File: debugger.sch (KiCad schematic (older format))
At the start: 12 parts, among them J2 USB_B_Micro, J5 Conn_ARM_JTAG_SWD_10, J6 Conn_ARM_JTAG_SWD_10, U7 STM32F042F6Px

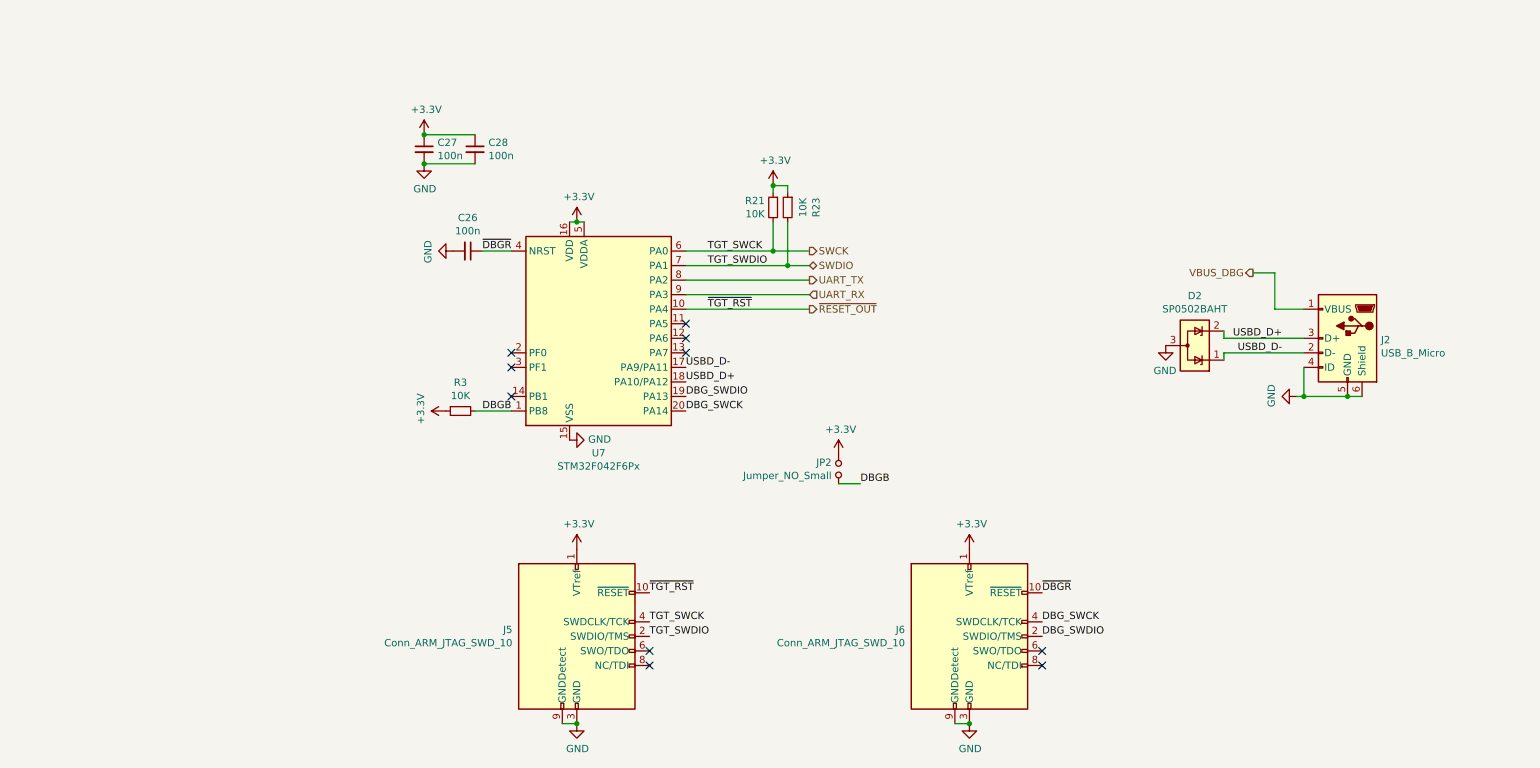
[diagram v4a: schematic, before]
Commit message: Replace STM32F042 in TSSOP by STM32F04[28] in QFN28
Others changes:

 - Export gerbers to current status
 - Update schematic export in svg and pdf
 - Update README image
 - Rename `USB OTG` sheet to `USB_OTG`

Signed-off-by: Martin Ribelotta <martinribelotta@gmail.com>
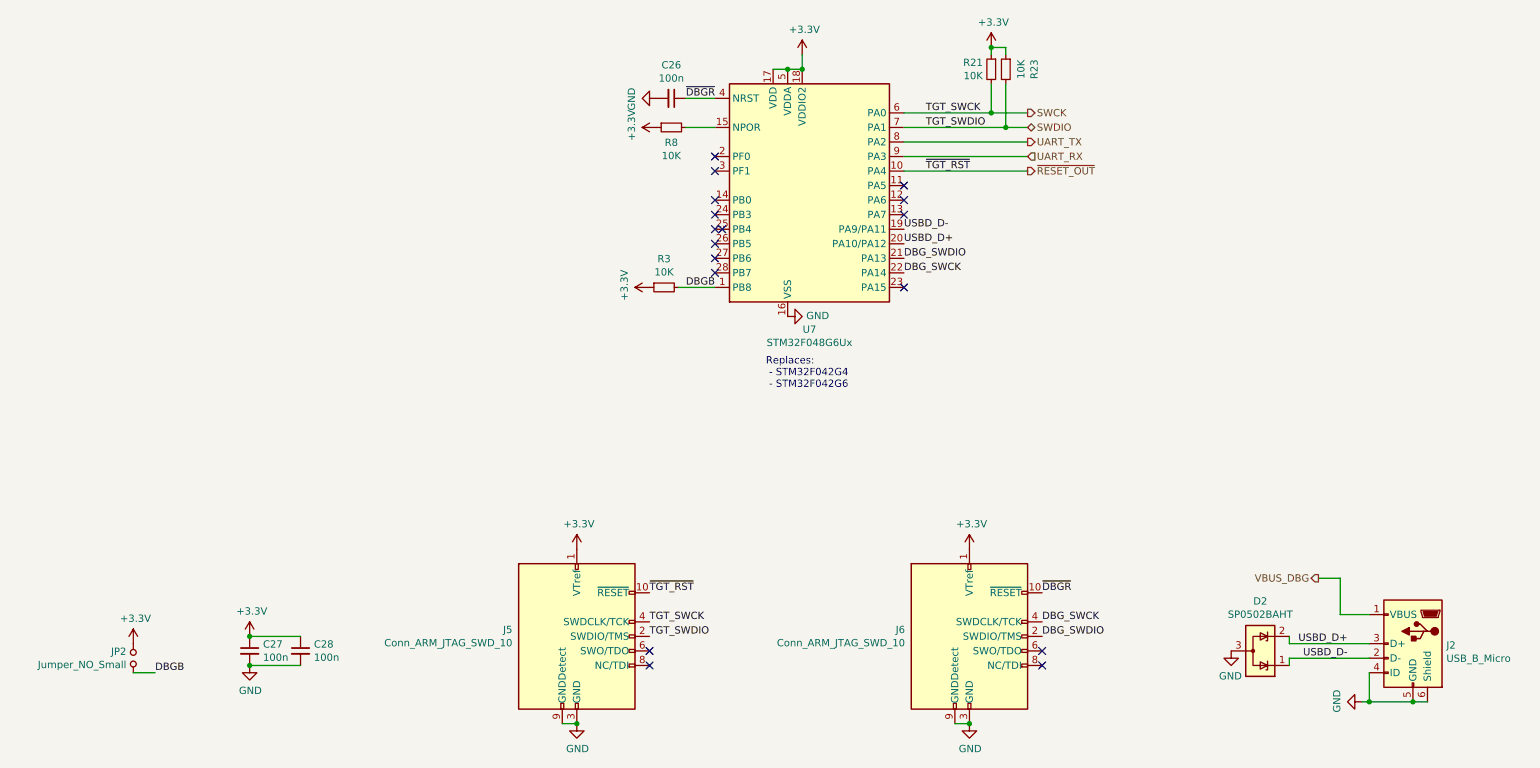
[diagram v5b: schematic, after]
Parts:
- removed U7: STM32F042F6Px, Package_SO:TSSOP-20_4.4x6.5mm_P0.65mm, symbol MCU_ST_STM32F0:STM32F042F6Px
- added R8: 10K, Resistor_SMD:R_0603_1608Metric, symbol Device:R_Small
- added U7: STM32F048G6Ux, Package_DFN_QFN:QFN-28_4x4mm_P0.5mm, symbol MCU_ST_STM32F0:STM32F048G6Ux
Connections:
- net +3V3: now also R8.1, U7.17 (VDD), U7.18 (VDDIO2), U7.5 (VDDA)
- net DBGB: now also U7.1 (PB8)
- net DBG_SWCK: now also U7.22 (PA14)
- net DBG_SWDIO: now also U7.21 (PA13)
- net GND: now also U7.16 (VSS)
- net SWCK: now also U7.6 (PA0)
- net SWDIO: now also U7.7 (PA1)
- net UART_RX: now also U7.9 (PA3)
- net UART_TX: now also U7.8 (PA2)
- net USBD_D+: now also U7.20 (PA10/PA12)
- net USBD_D-: now also U7.19 (PA9/PA11)
- net ~DBGR: now also U7.4 (NRST)
- net ~RESET_OUT: now also U7.10 (PA4)
- new net: R8.2, U7.15 (NPOR)
- no-connect marks 10 -> 17
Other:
- note added: "Replaces:\n - STM32F042G4\n - STM32F042G6\n"
- moved on the sheet: C26, C27, C28, D2, J2, JP2, R21, R23, R3

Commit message: Save point
Signed-off-by: Martin Ribelotta <martinribelotta@gmail.com>
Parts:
- added R10: 10K, Resistor_SMD:R_0603_1608Metric, symbol Device:R_Small
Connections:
- net +3V3: now also R10.1
- net ~DBGR: now also R10.2
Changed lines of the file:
@@
 Wire Wire Line
 	5350 1950 5150 1950
+$Comp
+L Device:R_Small R?
+U 1 1 606425AD
+P 5050 1400
+AR Path="/606425AD" Ref="R?"  Part="1"
+AR Path="/60158DDC/606425AD" Ref="R10"  Part="1"
+F 0 "R10" V 4854 1400 50  0000 C CNN
+F 1 "10K" V 4945 1400 50  0000 C CNN
+F 2 "Resistor_SMD:R_0603_1608Metric" H 5050 1400 50  0001 C CNN
+F 3 "~" H 5050 1400 50  0001 C CNN
+F 4 "Resistor 1.5K 0603" H 5050 1400 50  0001 C CNN "DESCRIPTION"
+F 5 "Yageo" H 5050 1400 50  0001 C CNN "MANUFACTURER"
+F 6 "RC0603FR-0710KL" H 5050 1400 50  0001 C CNN "MANUFACTURER_PART_NUMBER"
+	1    5050 1400
+	0    -1   1    0
+$EndComp
+$Comp
+L power:+3V3 #PWR?
+U 1 1 60642CCB
+P 4950 1400
+AR Path="/60642CCB" Ref="#PWR?"  Part="1"
+AR Path="/60158DDC/60642CCB" Ref="#PWR063"  Part="1"
+F 0 "#PWR063" H 4950 1250 50  0001 C CNN
+F 1 "+3.3V" H 4965 1573 50  0000 C CNN
+F 2 "" H 4950 1400 50  0000 C CNN
+F 3 "" H 4950 1400 50  0000 C CNN
+	1    4950 1400
+	0    -1   -1   0
+$EndComp
+Wire Wire Line
+	5150 1400 5350 1400
+Wire Wire Line
+	5350 1400 5350 1750
+Connection ~ 5350 1750
 $EndSCHEMATC

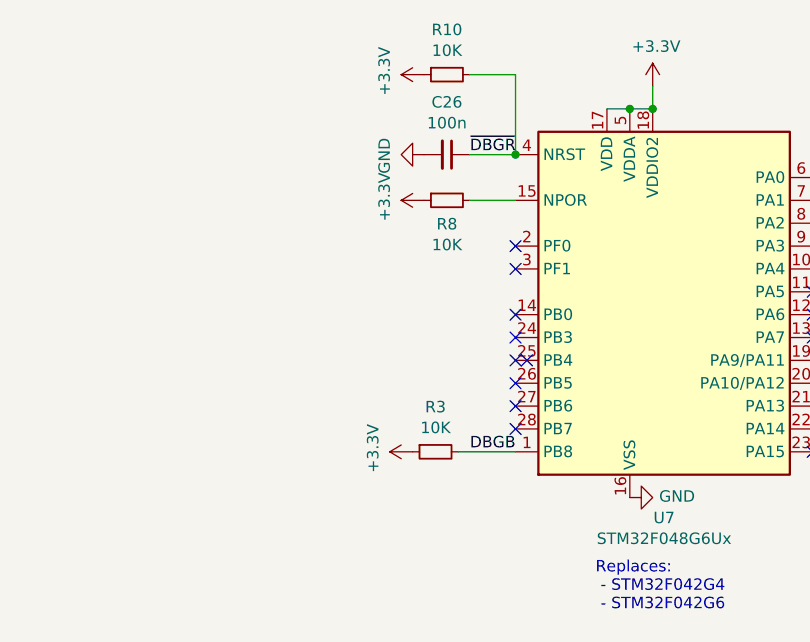
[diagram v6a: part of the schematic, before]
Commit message: Change QSPI PSRAM to hyperRAM
 - Replace QSPI PSRAM to HyperBUS version due to erratasheet
   of mcu (cannot write in QSPI mode without DQS and DQS not
   work in 4bit mode)
 - Connect hyperram to QSPI interface 2
 - Move QSPI flash to interface 1
 - Rearrangue pinouts due to new functionality
 - Remove extra pinouts (now all pins are in arduino connector9
 - Improve schematic and libreries to pass ERC
 - Add pin-1 mark on all IC

Signed-off-by: Martin Ribelotta <martinribelotta@gmail.com>
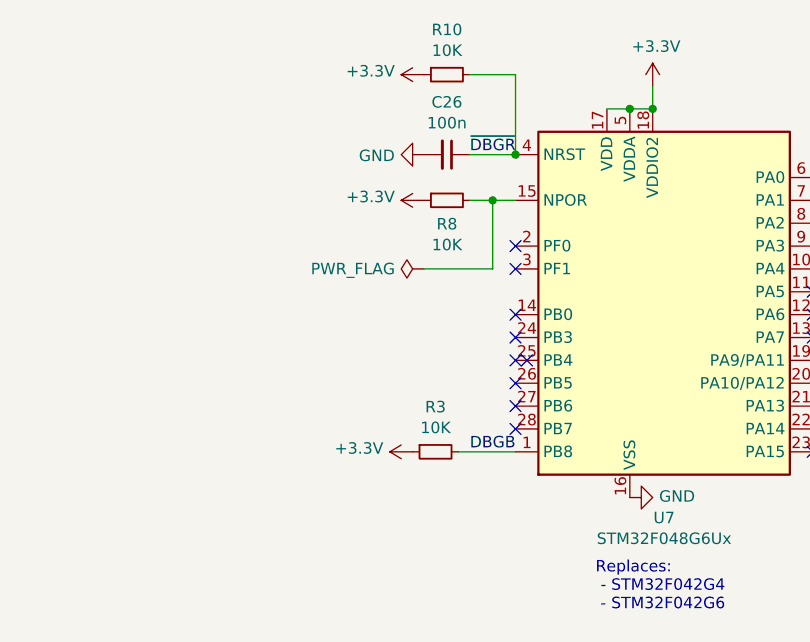
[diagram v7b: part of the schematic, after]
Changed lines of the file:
@@
 AR Path="/60158DDC/60186733" Ref="#PWR038"  Part="1"
 F 0 "#PWR038" H 4950 1500 50  0001 C CNN
-F 1 "GND" H 4955 1577 50  0000 C CNN
+F 1 "GND" V 4955 1622 50  0000 R CNN
 F 2 "" H 4950 1750 50  0000 C CNN
 F 3 "" H 4950 1750 50  0000 C CNN
@@
 AR Path="/60158DDC/6018A493" Ref="#PWR037"  Part="1"
 F 0 "#PWR037" H 4900 2900 50  0001 C CNN
-F 1 "+3.3V" H 4915 3223 50  0000 C CNN
+F 1 "+3.3V" V 4915 3178 50  0000 L CNN
 F 2 "" H 4900 3050 50  0000 C CNN
 F 3 "" H 4900 3050 50  0000 C CNN
@@
 AR Path="/60158DDC/605D4353" Ref="#PWR018"  Part="1"
 F 0 "#PWR018" H 4950 1800 50  0001 C CNN
-F 1 "+3.3V" H 4965 2123 50  0000 C CNN
+F 1 "+3.3V" V 4965 2078 50  0000 L CNN
 F 2 "" H 4950 1950 50  0000 C CNN
 F 3 "" H 4950 1950 50  0000 C CNN
@@
 $EndComp
 Wire Wire Line
-	5350 1950 5150 1950
+	5350 1950 5250 1950
 $Comp
 L Device:R_Small R?
@@
 AR Path="/60158DDC/60642CCB" Ref="#PWR063"  Part="1"
 F 0 "#PWR063" H 4950 1250 50  0001 C CNN
-F 1 "+3.3V" H 4965 1573 50  0000 C CNN
+F 1 "+3.3V" V 4965 1528 50  0000 L CNN
 F 2 "" H 4950 1400 50  0000 C CNN
 F 3 "" H 4950 1400 50  0000 C CNN
@@
 	5350 1400 5350 1750
 Connection ~ 5350 1750
+$Comp
+L power:PWR_FLAG #FLG?
+U 1 1 607D1E26
+P 4950 2250
+AR Path="/607D1E26" Ref="#FLG?"  Part="1"
+AR Path="/60158DDC/607D1E26" Ref="#FLG0108"  Part="1"
+F 0 "#FLG0108" H 4950 2325 50  0001 C CNN
+F 1 "PWR_FLAG" V 4950 2377 50  0000 L CNN
+F 2 "" H 4950 2250 50  0001 C CNN
+F 3 "~" H 4950 2250 50  0001 C CNN
+	1    4950 2250
+	0    -1   -1   0
+$EndComp
+Wire Wire Line
+	4950 2250 5250 2250
+Wire Wire Line
+	5250 2250 5250 1950
+Connection ~ 5250 1950
+Wire Wire Line
+	5250 1950 5150 1950
 $EndSCHEMATC

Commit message: Prepare for send to PCBWay
Signed-off-by: Martin Ribelotta <martinribelotta@gmail.com>
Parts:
- R10, R21, R23, R3, R8: DESCRIPTION Resistor 1.5K 0603 -> Resistor 10K 0603
- U7: DESCRIPTION (none) -> STM32F048G6Ux; MANUFACTURER (none) -> STMicroelectronics; MANUFACTURER_PART_NUMBER (none) -> STM32F048G6Ux
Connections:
- net +3V3: no longer R3.1
- net GND: now also R3.1
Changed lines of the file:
@@
 F 2 "Resistor_SMD:R_0603_1608Metric" H 5000 3050 50  0001 C CNN
 F 3 "~" H 5000 3050 50  0001 C CNN
-F 4 "Resistor 1.5K 0603" H 5000 3050 50  0001 C CNN "DESCRIPTION"
+F 4 "Resistor 10K 0603" H 5000 3050 50  0001 C CNN "DESCRIPTION"
 F 5 "Yageo" H 5000 3050 50  0001 C CNN "MANUFACTURER"
 F 6 "RC0603FR-0710KL" H 5000 3050 50  0001 C CNN "MANUFACTURER_PART_NUMBER"
 	1    5000 3050
 	0    -1   1    0
-$EndComp
-$Comp
-L power:+3V3 #PWR?
-U 1 1 6018A493
-P 4900 3050
-AR Path="/6018A493" Ref="#PWR?"  Part="1"
-AR Path="/60158DDC/6018A493" Ref="#PWR037"  Part="1"
-F 0 "#PWR037" H 4900 2900 50  0001 C CNN
-F 1 "+3.3V" V 4915 3178 50  0000 L CNN
-F 2 "" H 4900 3050 50  0000 C CNN
-F 3 "" H 4900 3050 50  0000 C CNN
-	1    4900 3050
-	0    -1   -1   0
 $EndComp
 Wire Wire Line
@@
 F 2 "Resistor_SMD:R_0603_1608Metric" H 7350 1550 50  0001 C CNN
 F 3 "~" H 7350 1550 50  0001 C CNN
-F 4 "Resistor 1.5K 0603" H 7350 1550 50  0001 C CNN "DESCRIPTION"
+F 4 "Resistor 10K 0603" H 7350 1550 50  0001 C CNN "DESCRIPTION"
 F 5 "Yageo" H 7350 1550 50  0001 C CNN "MANUFACTURER"
 F 6 "RC0603FR-0710KL" H 7350 1550 50  0001 C CNN "MANUFACTURER_PART_NUMBER"
@@
 F 2 "Resistor_SMD:R_0603_1608Metric" H 7250 1550 50  0001 C CNN
 F 3 "~" H 7250 1550 50  0001 C CNN
-F 4 "Resistor 1.5K 0603" H 7250 1550 50  0001 C CNN "DESCRIPTION"
+F 4 "Resistor 10K 0603" H 7250 1550 50  0001 C CNN "DESCRIPTION"
 F 5 "Yageo" H 7250 1550 50  0001 C CNN "MANUFACTURER"
 F 6 "RC0603FR-0710KL" H 7250 1550 50  0001 C CNN "MANUFACTURER_PART_NUMBER"
@@
 F 2 "Package_DFN_QFN:QFN-28_4x4mm_P0.5mm" H 5450 1550 50  0001 R CNN
 F 3 "http://www.st.com/st-web-ui/static/active/en/resource/technical/document/datasheet/DM00109264.pdf" H 6050 2350 50  0001 C CNN
+F 4 "STMicroelectronics" H 6050 2350 50  0001 C CNN "MANUFACTURER"
+F 5 "STM32F048G6Ux" H 6050 2350 50  0001 C CNN "MANUFACTURER_PART_NUMBER"
+F 6 "STM32F048G6Ux" H 6050 2350 50  0001 C CNN "DESCRIPTION"
 	1    6050 2350
 	1    0    0    -1
@@
 F 2 "Resistor_SMD:R_0603_1608Metric" H 5050 1950 50  0001 C CNN
 F 3 "~" H 5050 1950 50  0001 C CNN
-F 4 "Resistor 1.5K 0603" H 5050 1950 50  0001 C CNN "DESCRIPTION"
+F 4 "Resistor 10K 0603" H 5050 1950 50  0001 C CNN "DESCRIPTION"
 F 5 "Yageo" H 5050 1950 50  0001 C CNN "MANUFACTURER"
 F 6 "RC0603FR-0710KL" H 5050 1950 50  0001 C CNN "MANUFACTURER_PART_NUMBER"
@@
 F 2 "Resistor_SMD:R_0603_1608Metric" H 5050 1400 50  0001 C CNN
 F 3 "~" H 5050 1400 50  0001 C CNN
-F 4 "Resistor 1.5K 0603" H 5050 1400 50  0001 C CNN "DESCRIPTION"
+F 4 "Resistor 10K 0603" H 5050 1400 50  0001 C CNN "DESCRIPTION"
 F 5 "Yageo" H 5050 1400 50  0001 C CNN "MANUFACTURER"
 F 6 "RC0603FR-0710KL" H 5050 1400 50  0001 C CNN "MANUFACTURER_PART_NUMBER"
@@
 Wire Wire Line
 	5250 1950 5150 1950
+$Comp
+L power:GND #PWR?
+U 1 1 608F7DDB
+P 4900 3050
+AR Path="/608F7DDB" Ref="#PWR?"  Part="1"
+AR Path="/60158DDC/608F7DDB" Ref="#PWR?"  Part="1"
+F 0 "#PWR?" H 4900 2800 50  0001 C CNN
+F 1 "GND" V 4905 2922 50  0000 R CNN
+F 2 "" H 4900 3050 50  0000 C CNN
+F 3 "" H 4900 3050 50  0000 C CNN
+	1    4900 3050
+	0    1    1    0
+$EndComp
 $EndSCHEMATC
